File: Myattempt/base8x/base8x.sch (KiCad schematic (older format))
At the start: 59 parts, among them J1 Conn_02x05_Odd_Even, J10 Conn_02x14_Counter_Clockwise, J10 Conn_02x20_Odd_Even, J11 Conn_02x14_Counter_Clockwise, J12 Conn_02x14_Counter_Clockwise, J13 Conn_02x14_Counter_Clockwise, J14 Conn_02x14_Counter_Clockwise, J15 Conn_02x14_Counter_Clockwise, J16 Conn_01x14, J2 GS3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

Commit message: My work implementing resistor for sensor
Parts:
- removed J10, J11, J12, J13, J14, J15: Conn_02x14_Counter_Clockwise, Connector_PinSocket_2.54mm:PinSocket_2x14_P2.54mm_Vertical, symbol Connector_Generic:Conn_02x14_Odd_Even
- removed J16: Conn_01x14, Connector_PinSocket_2.54mm:PinSocket_1x14_P2.54mm_Vertical, symbol Connector_Generic:Conn_01x14
- added Resistor1: 4.7k, Resistor_THT:R_Axial_DIN0617_L17.0mm_D6.0mm_P20.32mm_Horizontal, symbol Device:R
- added Temp_sensor1: Conn_01x03_Female, Connector_PinSocket_2.54mm:PinSocket_1x03_P2.54mm_Vertical, symbol Connector:Conn_01x03_Female
- J9: symbol base8x-rescue:Screw_Terminal_01x08-Connector_Specialized -> base8x-rescue:Screw_Terminal_01x08-Connector_Specialized-base8x-rescue
- L1: symbol base8x-rescue:GREY@CHRISTOFORO.NET-myParts -> base8x-rescue:GREY@CHRISTOFORO.NET-myParts-base8x-rescue
- MK1, MK2: symbol base8x-rescue:Mounting_Hole_PAD-Mechanical -> base8x-rescue:Mounting_Hole_PAD-Mechanical-base8x-rescue
- MK10, MK11, MK12, MK13, MK14, MK15, MK16, MK17, MK18, MK19, MK20, MK3, MK4, MK5, MK6, MK7, MK8, MK9: symbol base8x-rescue:Mounting_Hole-Mechanical -> base8x-rescue:Mounting_Hole-Mechanical-base8x-rescue
- Raspberry_header1: renamed from J10; footprint (none) -> Connector_PinSocket_2.54mm:PinSocket_2x20_P2.54mm_Vertical
- TP1, TP2, TP3, TP4, TP5, TP6: symbol base8x-rescue:Test_Point-Connector_Specialized -> base8x-rescue:Test_Point-Connector_Specialized-base8x-rescue
- U1: symbol myParts:ADS1115 -> base8x-rescue:ADS1115-myParts
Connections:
- net labels added: CLK0
- wire segments 117 -> 100
- no-connect marks 221 -> 78
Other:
- note removed: "B"
- note removed: "C"
- note removed: "C-B"
- note removed: "D"
- note removed: "D-C"
- note removed: "E"
- note removed: "E-D"
- note removed: "F"
- note removed: "F-E"
- note removed: "G"
- note removed: "G-F"
- note removed: "H"
- note removed: "H-G"
- note removed: "X-H"
- moved on the sheet: Raspberry_header1

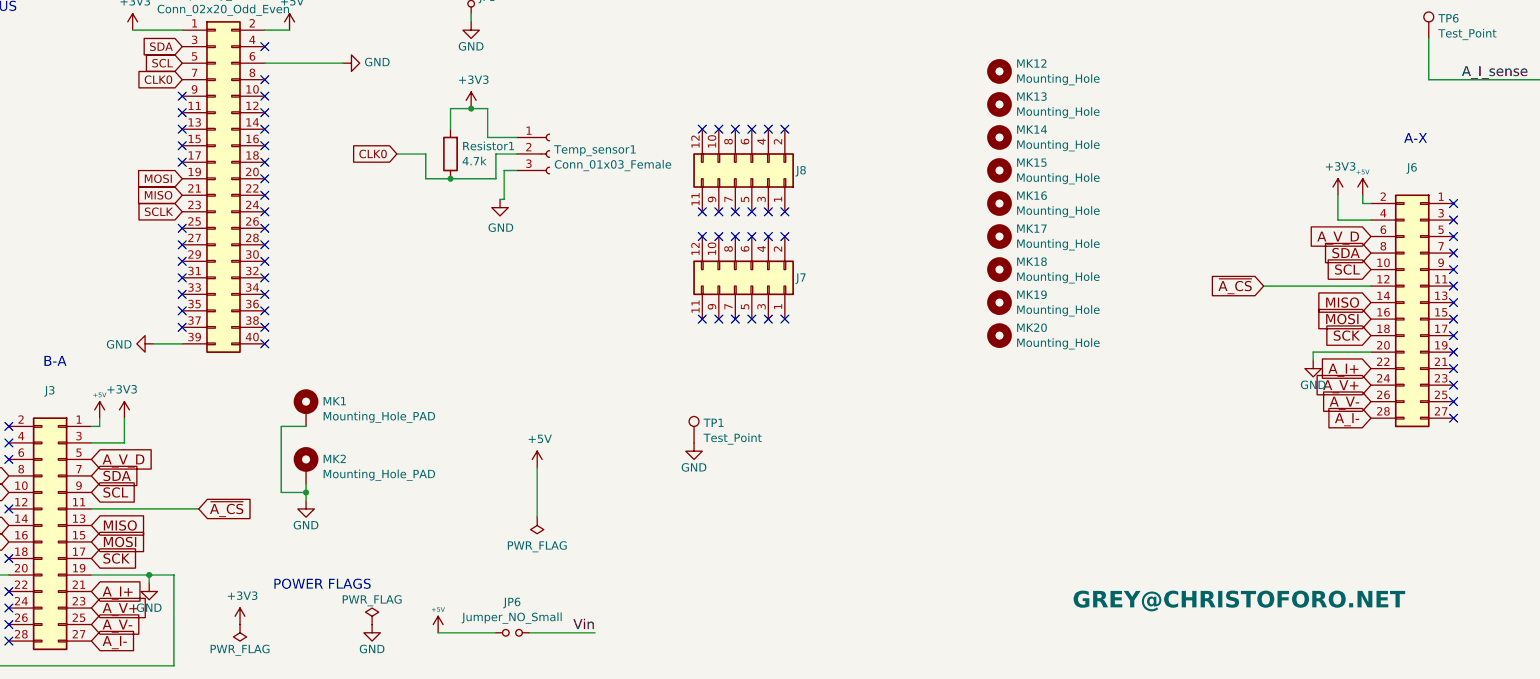
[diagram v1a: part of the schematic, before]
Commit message: adding ssr and sensor
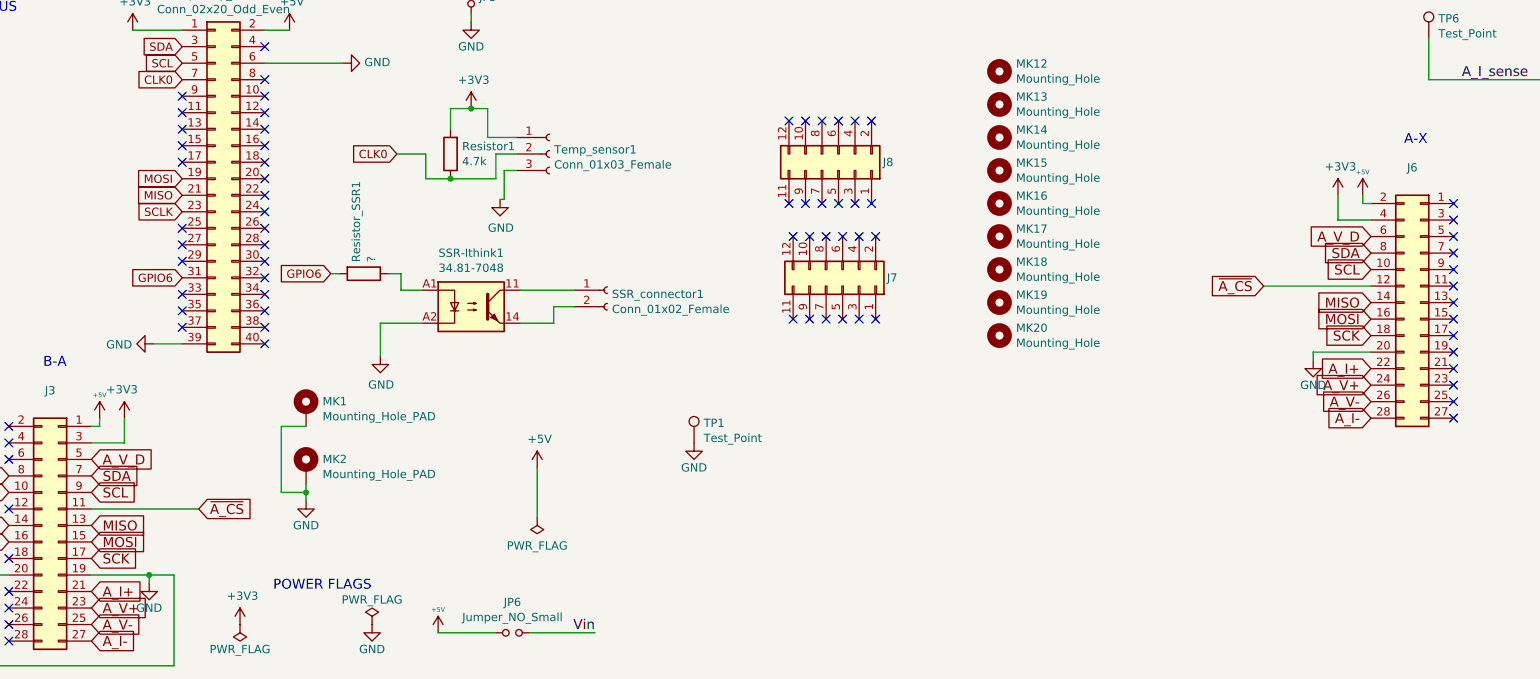
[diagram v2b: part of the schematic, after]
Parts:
- removed L1: GREY@CHRISTOFORO.NET, myParts:logo, symbol base8x-rescue:GREY@CHRISTOFORO.NET-myParts-base8x-rescue
- added Resistor_SSR1: ?, Resistor_THT:R_Axial_DIN0617_L17.0mm_D6.0mm_P20.32mm_Horizontal, symbol Device:R
- added SSR-Ithink1: 34.81-7048, OptoDevice:Finder_34.81, symbol Relay_SolidState:34.81-7048
- added SSR_connector1: Conn_01x02_Female, Connector_PinSocket_2.54mm:PinSocket_1x02_P2.54mm_Vertical, symbol Connector:Conn_01x02_Female
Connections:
- net labels added: GPIO6
- wire segments 100 -> 110
- no-connect marks 78 -> 77
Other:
- moved on the sheet: J7, J8
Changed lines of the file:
@@
 A_V+
-$Comp
-L base8x-rescue:GREY@CHRISTOFORO.NET-myParts-base8x-rescue L1
-U 1 1 59B41702
-P 8950 7250
-F 0 "L1" H 8950 7125 60  0001 C CNN
-F 1 "GREY@CHRISTOFORO.NET" H 8950 7250 100 0000 C CNB
-F 2 "myParts:logo" H 8950 7250 60  0001 C CNN
-F 3 "" H 8950 7250 60  0001 C CNN
-	1    8950 7250
-	1    0    0    -1
-$EndComp
 $Comp
 L Connector_Generic:Conn_02x14_Odd_Even J3
@@
 	3150 6200 3150 6600
 $Comp
-L Connector_Generic:Conn_02x06_Odd_Even J7
-U 1 1 59F46AAD
-P 6000 5350
-F 0 "J7" V 6050 5650 50  0000 C CNN
-F 1 "Conn_02x06_Counter_Clockwise" H 6050 5676 50  0001 C CNN
-F 2 "Connector_PinHeader_2.54mm:PinHeader_2x06_P2.54mm_Vertical" H 6000 5350 50  0001 C CNN
-F 3 "" H 6000 5350 50  0001 C CNN
-	1    6000 5350
-	0    1    -1   0
-$EndComp
-$Comp
 L Connector_Generic:Conn_02x06_Odd_Even J8
 U 1 1 59F46B55
-P 6000 4700
-F 0 "J8" V 6050 5000 50  0000 C CNN
-F 1 "Conn_02x06_Counter_Clockwise" H 6050 5026 50  0001 C CNN
-F 2 "Connector_PinHeader_2.54mm:PinHeader_2x06_P2.54mm_Vertical" H 6000 4700 50  0001 C CNN
-F 3 "" H 6000 4700 50  0001 C CNN
-	1    6000 4700
+P 6525 4650
+F 0 "J8" V 6575 4950 50  0000 C CNN
+F 1 "Conn_02x06_Counter_Clockwise" H 6575 4976 50  0001 C CNN
+F 2 "Connector_PinHeader_2.54mm:PinHeader_2x06_P2.54mm_Vertical" H 6525 4650 50  0001 C CNN
+F 3 "" H 6525 4650 50  0001 C CNN
+	1    6525 4650
 	0    1    -1   0
 $EndComp
-NoConn ~ 6200 4900
-NoConn ~ 6100 4900
-NoConn ~ 6000 4900
-NoConn ~ 5900 4900
-NoConn ~ 5800 4900
-NoConn ~ 5700 4900
-NoConn ~ 5700 4400
-NoConn ~ 5800 4400
-NoConn ~ 5900 4400
-NoConn ~ 6000 4400
-NoConn ~ 6100 4400
-NoConn ~ 6200 4400
-NoConn ~ 6200 5050
-NoConn ~ 6100 5050
-NoConn ~ 6000 5050
-NoConn ~ 5900 5050
-NoConn ~ 5800 5050
-NoConn ~ 5700 5050
-NoConn ~ 5700 5550
-NoConn ~ 5800 5550
-NoConn ~ 5900 5550
-NoConn ~ 6000 5550
-NoConn ~ 6100 5550
-NoConn ~ 6200 5550
+NoConn ~ 6725 4850
+NoConn ~ 6625 4850
+NoConn ~ 6525 4850
+NoConn ~ 6425 4850
+NoConn ~ 6325 4850
+NoConn ~ 6225 4850
+NoConn ~ 6225 4350
+NoConn ~ 6325 4350
+NoConn ~ 6425 4350
+NoConn ~ 6525 4350
+NoConn ~ 6625 4350
+NoConn ~ 6725 4350
+NoConn ~ 6750 5050
+NoConn ~ 6650 5050
+NoConn ~ 6550 5050
+NoConn ~ 6450 5050
+NoConn ~ 6350 5050
+NoConn ~ 6250 5050
+NoConn ~ 6250 5550
+NoConn ~ 6350 5550
+NoConn ~ 6450 5550
+NoConn ~ 6550 5550
+NoConn ~ 6650 5550
+NoConn ~ 6750 5550
 $Comp
 L Connector_Generic:Conn_02x05_Odd_Even J1
@@
 NoConn ~ 2550 5100
 NoConn ~ 2550 5200
-NoConn ~ 2550 5300
 NoConn ~ 2550 5400
 NoConn ~ 2550 5500
@@
 	4025 4700 4025 4550
 Connection ~ 4175 4700
+$Comp
+L Relay_SolidState:34.81-7048 SSR-Ithink1
+U 1 1 6011EB5B
+P 4300 5475
+F 0 "SSR-Ithink1" H 4300 5800 50  0000 C CNN
+F 1 "34.81-7048" H 4300 5709 50  0000 C CNN
+F 2 "OptoDevice:Finder_34.81" H 4100 5275 50  0001 L CIN
+F 3 "http://www.us.liteon.com/downloads/LTV-817-827-847.PDF" H 4300 5475 50  0001 L CNN
+	1    4300 5475
+	1    0    0    -1
+$EndComp
+$Comp
+L Connector:Conn_01x02_Female SSR_connector1
+U 1 1 60124448
+P 5125 5375
+F 0 "SSR_connector1" H 5153 5351 50  0000 L CNN
+F 1 "Conn_01x02_Female" H 5153 5260 50  0000 L CNN
+F 2 "Connector_PinSocket_2.54mm:PinSocket_1x02_P2.54mm_Vertical" H 5125 5375 50  0001 C CNN
+F 3 "~" H 5125 5375 50  0001 C CNN
+	1    5125 5375
+	1    0    0    -1
+$EndComp
+Wire Wire Line
+	4600 5575 4800 5575
+Wire Wire Line
+	4800 5575 4800 5475
+Wire Wire Line
+	4800 5475 4925 5475
+Wire Wire Line
+	4000 5575 3750 5575
+Wire Wire Line
+	3750 5575 3750 5775
+$Comp
+L power:GND #PWR0107
+U 1 1 6012CB70
+P 3750 5775
+F 0 "#PWR0107" H 3750 5525 50  0001 C CNN
+F 1 "GND" H 3755 5602 50  0000 C CNN
+F 2 "" H 3750 5775 50  0001 C CNN
+F 3 "" H 3750 5775 50  0001 C CNN
+	1    3750 5775
+	1    0    0    -1
+$EndComp
+Wire Wire Line
+	4000 5375 3875 5375
+Wire Wire Line
+	3875 5375 3875 5275
+Wire Wire Line
+	3875 5275 3800 5275
+$Comp
+L Device:R Resistor_SSR1
+U 1 1 60130DA5
+P 3650 5275
+F 0 "Resistor_SSR1" H 3580 5229 50  0000 R CNN
+F 1 "?" H 3580 5320 50  0000 R CNN
+F 2 "Resistor_THT:R_Axial_DIN0617_L17.0mm_D6.0mm_P20.32mm_Horizontal" V 3580 5275 50  0001 C CNN
+F 3 "~" H 3650 5275 50  0001 C CNN
+	1    3650 5275
+	0    1    1    0
+$EndComp
+Text GLabel 2550 5300 0    50   Input ~ 0
+GPIO6
+Text GLabel 3450 5275 0    50   Input ~ 0
+GPIO6
+Wire Wire Line
+	3450 5275 3500 5275
+$Comp
+L Connector_Generic:Conn_02x06_Odd_Even J7
+U 1 1 59F46AAD
+P 6550 5350
+F 0 "J7" V 6600 5650 50  0000 C CNN
+F 1 "Conn_02x06_Counter_Clockwise" H 6600 5676 50  0001 C CNN
+F 2 "Connector_PinHeader_2.54mm:PinHeader_2x06_P2.54mm_Vertical" H 6550 5350 50  0001 C CNN
+F 3 "" H 6550 5350 50  0001 C CNN
+	1    6550 5350
+	0    1    -1   0
+$EndComp
+Wire Wire Line
+	4600 5375 4925 5375
 $EndSCHEMATC

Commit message: ?
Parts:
- removed J6: Conn_02x14_Counter_Clockwise, Connector_PinSocket_2.54mm:PinSocket_2x14_P2.54mm_Vertical, symbol Connector_Generic:Conn_02x14_Odd_Even
- removed J7, J8: Conn_02x06_Counter_Clockwise, Connector_PinHeader_2.54mm:PinHeader_2x06_P2.54mm_Vertical, symbol Connector_Generic:Conn_02x06_Odd_Even
- removed MK12, MK13, MK14, MK15, MK16, MK17, MK18, MK19, MK20, MK5, MK7, MK8: Mounting_Hole, MountingHole:MountingHole_3.2mm_M3, symbol base8x-rescue:Mounting_Hole-Mechanical-base8x-rescue
- removed MK3, MK4: Mounting_Hole, MountingHole:MountingHole_6mm, symbol base8x-rescue:Mounting_Hole-Mechanical-base8x-rescue
- removed MK6: Mounting_Hole, MountingHole:MountingHole_4.3mm_M4, symbol base8x-rescue:Mounting_Hole-Mechanical-base8x-rescue
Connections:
- net GND: no longer J3.20 (Pin_20)
- net MISO: no longer J3.14 (Pin_14)
- net MOSI: no longer J3.16 (Pin_16)
- net SCK: now also Raspberry_header1.24 (Pin_24)
- net SCL: no longer J3.10 (Pin_10)
- net SDA: no longer J3.8 (Pin_8)
- no-connect marks 77 -> 44
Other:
- note removed: "A-X"
